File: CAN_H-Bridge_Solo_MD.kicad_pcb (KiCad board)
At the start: 2 copper layers, 84.3 x 40.1 mm, 46 parts, among them IC2 SI8650AB-B-IS1, IC3 A3921KLPTR-T, J1 Conn_01x03, J2 Conthrough, J3 Bus_mechaken_PCIexpress_x16_1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, M1 Motor_DC, Q1 TK6R7P06PLRQ, Q2 TK6R7P06PLRQ, Q3 TK6R7P06PLRQ, Q4 TK6R7P06PLRQ, U1 AP2210N-3.3TRG1, U2 STM32F303K8, U3 MCP1799T-3302H/TT, U4 MCP2562-E-SN

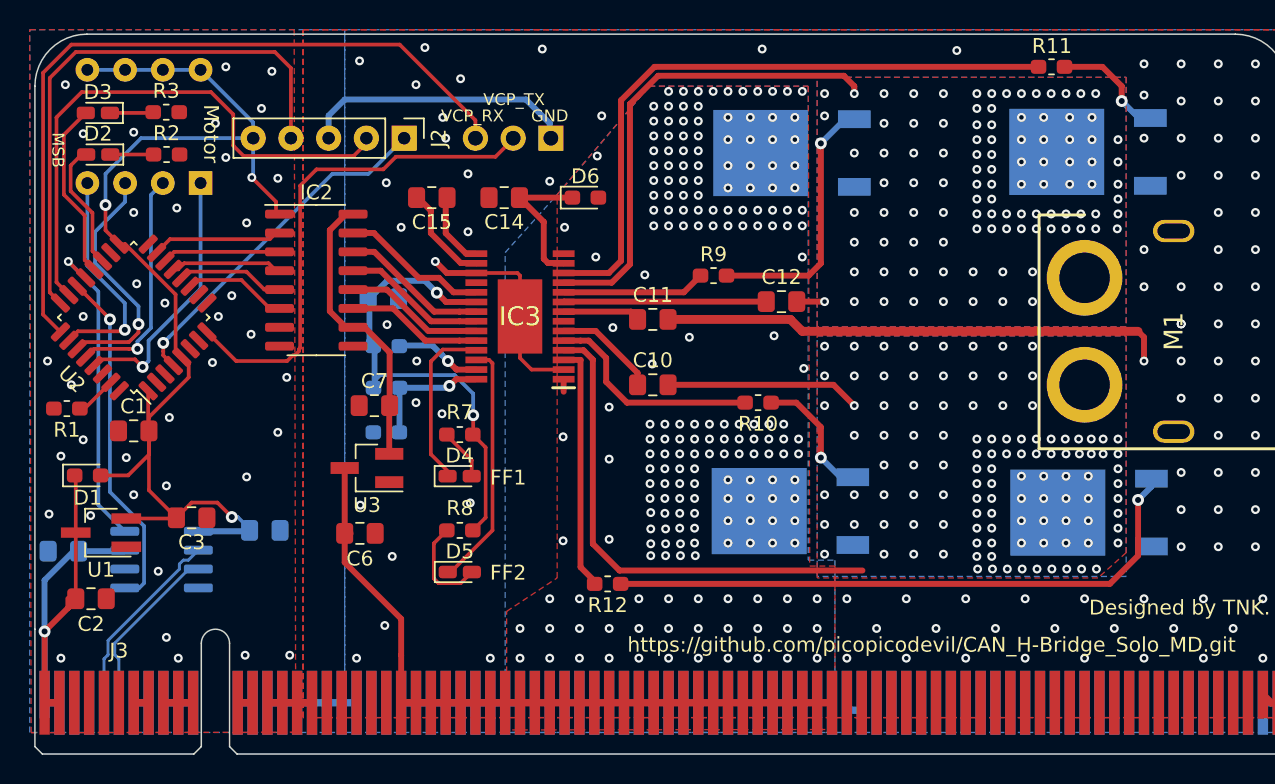
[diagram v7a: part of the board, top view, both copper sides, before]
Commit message: Update: エンコーダ対応
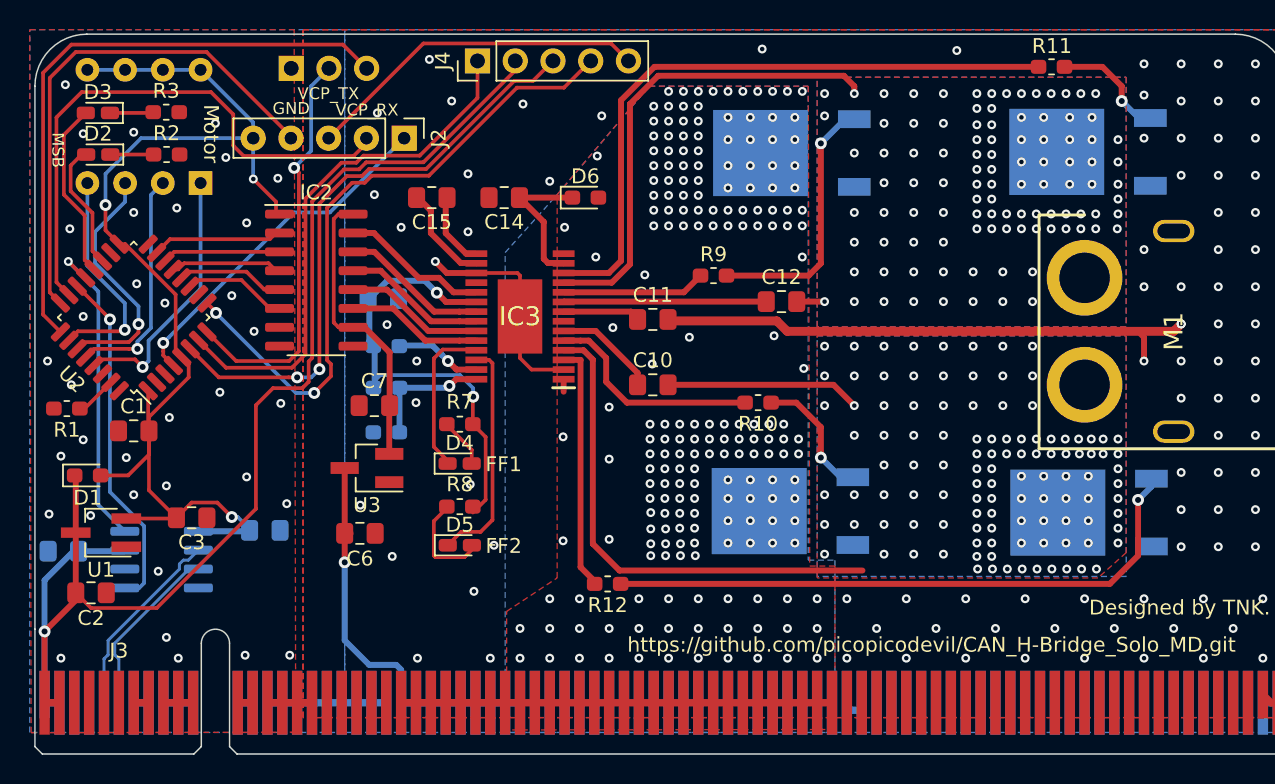
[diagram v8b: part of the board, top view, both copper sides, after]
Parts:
- added J4: Conn_01x05, Connector_PinHeader_2.54mm:PinHeader_1x05_P2.54mm_Vertical, F.Cu at (105.1, 114.8)
- C1, C13, C14, C8, C9: value 0.1uF -> 0.1u
- C10, C11, C12: value 4.7uF -> 4.7u
- C15: value 0.47uF -> 0.47u
- C2, C6, C7: value 1uF -> 1u
- C3: value 2.2uF -> 2.2u
- R10, R11, R12, R9: value 21 -> 30
- moved J1 18.1 mm to (92.6, 115.3), turned to 270 degrees
- moved D5 1.80 mm to (104.0, 147.4)
- moved R8 1.60 mm to (104.0, 144.8)
- moved D4 0.85 mm to (103.9, 141.9)
- moved R7 0.70 mm to (104.0, 139.2)
- moved C2 0.40 mm to (79.1, 150.6)
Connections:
- J3 pad A8: GNDPWR -> Net-(J3-PadA8)
- U2 pad 6: Net-(U2-Pad6) -> /ENC_A
- U2 pad 7: Net-(U2-Pad7) -> /ENC_B
- U2 pad 9: Net-(U2-Pad9) -> /ENC_X
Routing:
- net +5V: track 32.5 -> 90.0 mm
- net /ENC_X: track 0.00 -> 44.6 mm, vias 0 -> 2
- net /ENC_A: track 0.00 -> 40.6 mm, vias 0 -> 2
- net /ENC_B: track 0.00 -> 35.7 mm
- net VCP_RX: track 51.1 -> 41.2 mm
- net Net-(J3-PadA8): track 0.00 -> 8.00 mm
- net VCP_TX: track 34.1 -> 27.4 mm, vias 0 -> 1
- net GND: track 18.5 -> 23.3 mm, vias 39 -> 35
- net GNDPWR: track 61.3 -> 58.4 mm, vias 95 -> 92
- net /SWCLK: track 37.6 -> 34.9 mm
- net MD_FF2_0: track 16.6 -> 15.4 mm
- net VCC: track 55.7 -> 56.8 mm, vias 198 -> 199
- net V5: track 31.6 -> 30.7 mm
- net MD_FF1_0: track 11.7 -> 10.9 mm
- net MD_3V3: track 19.5 -> 20.1 mm
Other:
- board text added: "CAN H-Bridge Solo MD Prototype 3.0"
- board text removed: "CAN H-Bridge Solo MD Prototype 2.0"
